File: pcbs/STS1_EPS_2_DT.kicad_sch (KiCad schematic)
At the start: 23 parts, among them Q18 2N7002, Q19 SI7272DP-T1-GE3, Q20 2N7002, Q21 2N7002, U1 LTC6995IDCB-1, U2 4072

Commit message: Worked on STS1_EPS_2.
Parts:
- renumbered Q18 to Q1, Q19 to Q2, Q20 to Q3, Q21 to Q4, R6 to R1, R20 to R10, R21 to R11, R12 to R2, R13 to R3, R14 to R4, R15 to R5, R16 to R6, R17 to R7, R18 to R8, R19 to R9, TP5 to TP4, TP26 to TP5, U2 to U1, U1 to U2

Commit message: Worked on STS1_EPS_2.
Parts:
- removed Q1: 2N7002, Package_TO_SOT_SMD:SOT-23, symbol Transistor_FET:2N7002
- removed R3, R4, R6: 100k, Resistor_SMD:R_0805_2012Metric, symbol Device:R
- removed unit 1 of U1
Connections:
- net DS1_SIGNAL: now also U1.11
- net DS2_SIGNAL: now also U1.9
- net GND: no longer U1.11

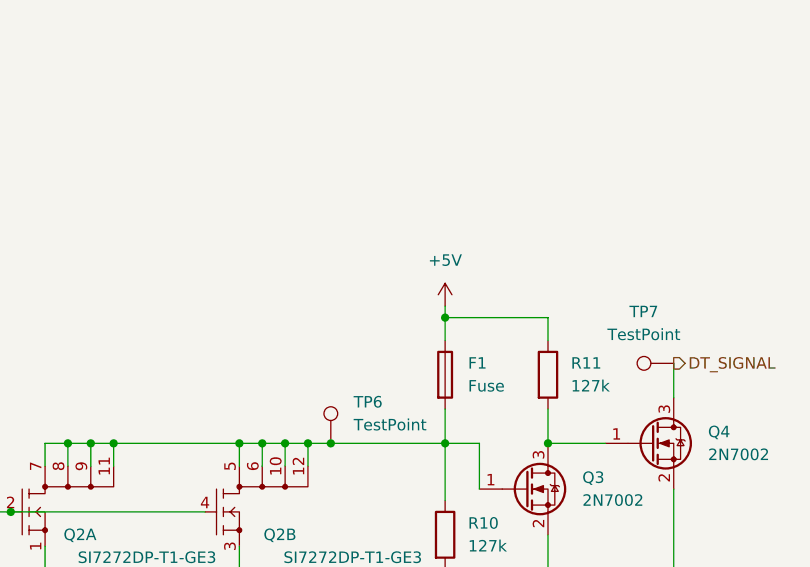
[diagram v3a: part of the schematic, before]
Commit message: Added a logic voltage, so that the deployment circuit breaker FETs also work, when battery is fails.
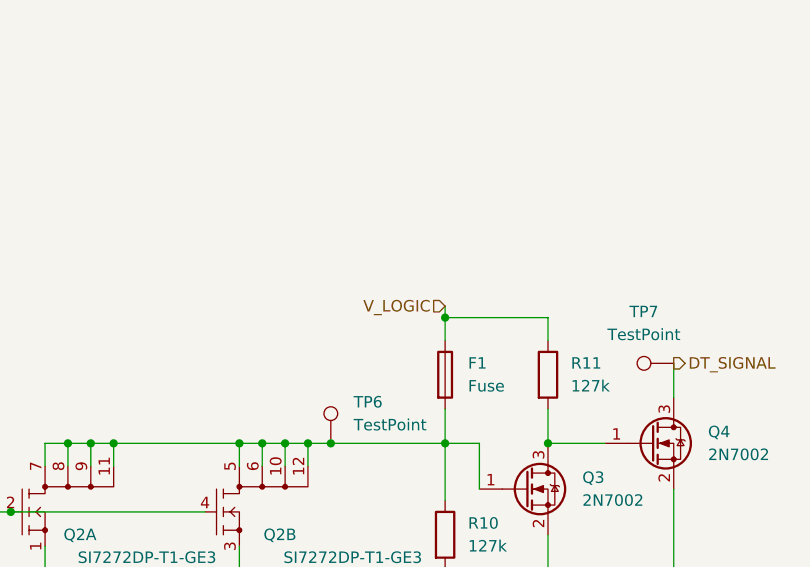
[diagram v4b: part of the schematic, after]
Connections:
- net +5V: no longer F1.1, R11.1
- new net V_LOGIC: F1.1, R11.1
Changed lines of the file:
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@@
+    (effects (font (size 1.27 1.27)) (justify right))
+  )
+  (hierarchical_label "V_LOGIC" (shape input) (at 241.3 67.31 180)
     (effects (font (size 1.27 1.27)) (justify right))
   )
@@
     (pin "6")
   )
-  (symbol (lib_id "power:+5V") (at 241.3 67.31 0) (unit 1)
-    (in_bom yes) (on_board yes) (fields_autoplaced)
-    (property "Reference" "#PWR0114" (id 0) (at 241.3 71.12 0)
-      (effects (font (size 1.27 1.27)) hide)
-    )
-    (property "Value" "+5V" (id 1) (at 241.3 62.23 0))
-    (property "Footprint" "" (id 2) (at 241.3 67.31 0)
-      (effects (font (size 1.27 1.27)) hide)
-    )
-    (property "Datasheet" "" (id 3) (at 241.3 67.31 0)
-      (effects (font (size 1.27 1.27)) hide)
-    )
-    (pin "1")
-  )
   (symbol (lib_id "power:+5V") (at 33.02 73.025 0) (unit 1)
